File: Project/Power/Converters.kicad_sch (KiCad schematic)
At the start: 24 parts, among them U15 TPS560200, U16 MIC5219-3.3YM5, U17 TPS562200

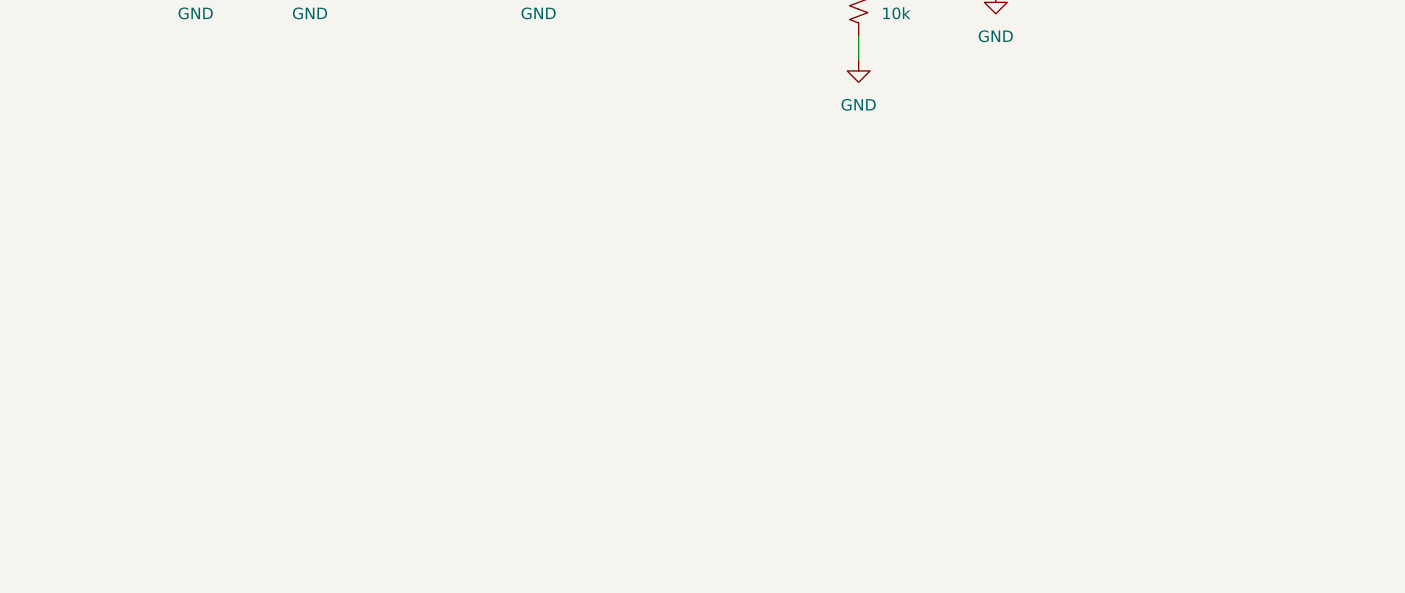
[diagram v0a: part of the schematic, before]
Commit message: Add 5V 6A voltage regulator
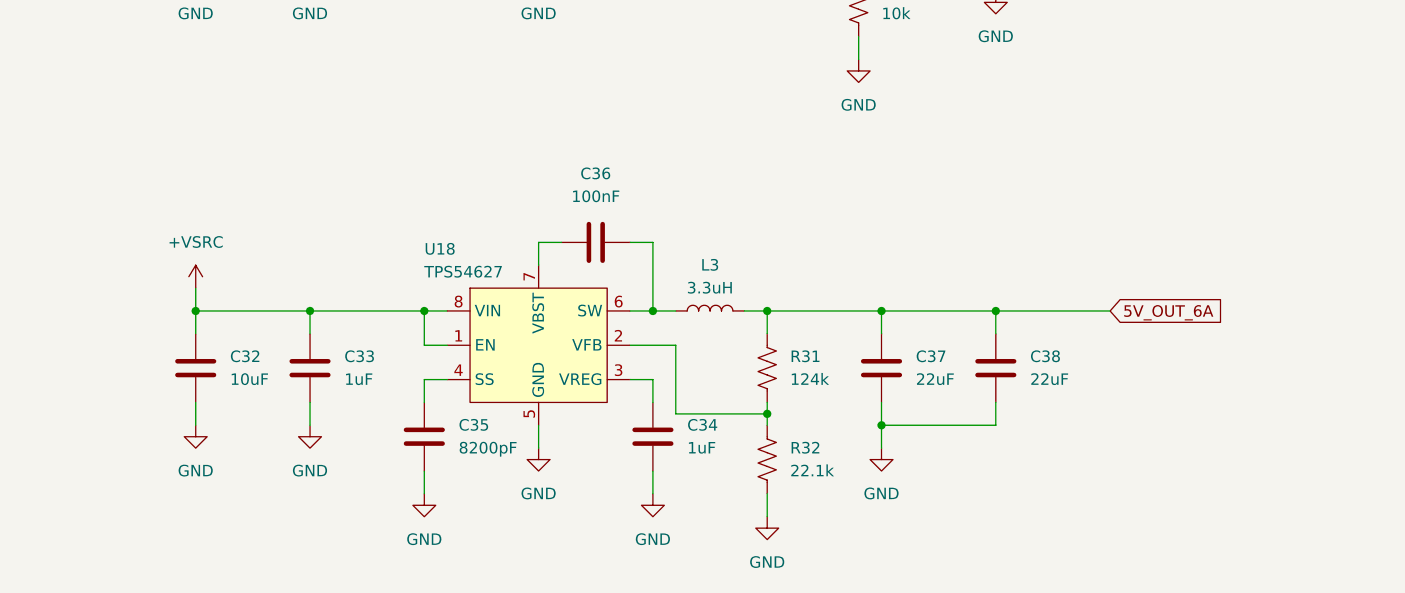
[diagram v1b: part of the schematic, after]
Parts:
- added C32: 10uF, Capacitor_SMD:C_1206_3216Metric, symbol Device:C
- added C33, C34: 1uF, Capacitor_SMD:C_0603_1608Metric, symbol Device:C
- added C35: 8200pF, Capacitor_SMD:C_0603_1608Metric, symbol Device:C
- added C36: 100nF, Capacitor_SMD:C_0603_1608Metric, symbol Device:C
- added C37, C38: 22uF, Capacitor_SMD:C_1206_3216Metric, symbol Device:C
- added L3: 3.3uH, Inductor_SMD:L_APV_APH0630, symbol Device:L
- added R31: 124k, Resistor_SMD:R_0603_1608Metric, symbol Device:R_US
- added R32: 22.1k, Resistor_SMD:R_0603_1608Metric, symbol Device:R_US
- added U18: TPS54627, Package_SO:SOIC-8-1EP_3.9x4.9mm_P1.27mm_EP2.95x4.9mm_Mask2.71x3.4mm_ThermalVias, symbol XuLab:TPS54627
- L2: footprint Inductor_SMD:L_Pulse_PA4340 -> Inductor_SMD:L_APV_APH0630; Listing https://www.digikey.com/en/products/detail/pulse-electronic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 -> https://www.digikey.com/en/products/detail/sumida-america-i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
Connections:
- net +VSRC: now also C32.1, C33.1, U18.1 (EN), U18.8 (VIN)
- net GND: now also C32.2, C33.2, C34.2, C35.2, C37.2, C38.2, R32.1, U18.5 (GND), U18.9 (GND)
- new net: R31.2, R32.2, U18.2 (VFB)
- new net: C34.1, U18.3 (VREG)
- new net: C35.1, U18.4 (SS)
- new net: C36.2, L3.1, U18.6 (SW)
- new net: C36.1, U18.7 (VBST)
- new net 5V_OUT_6A: C37.1, C38.1, L3.2, R31.1

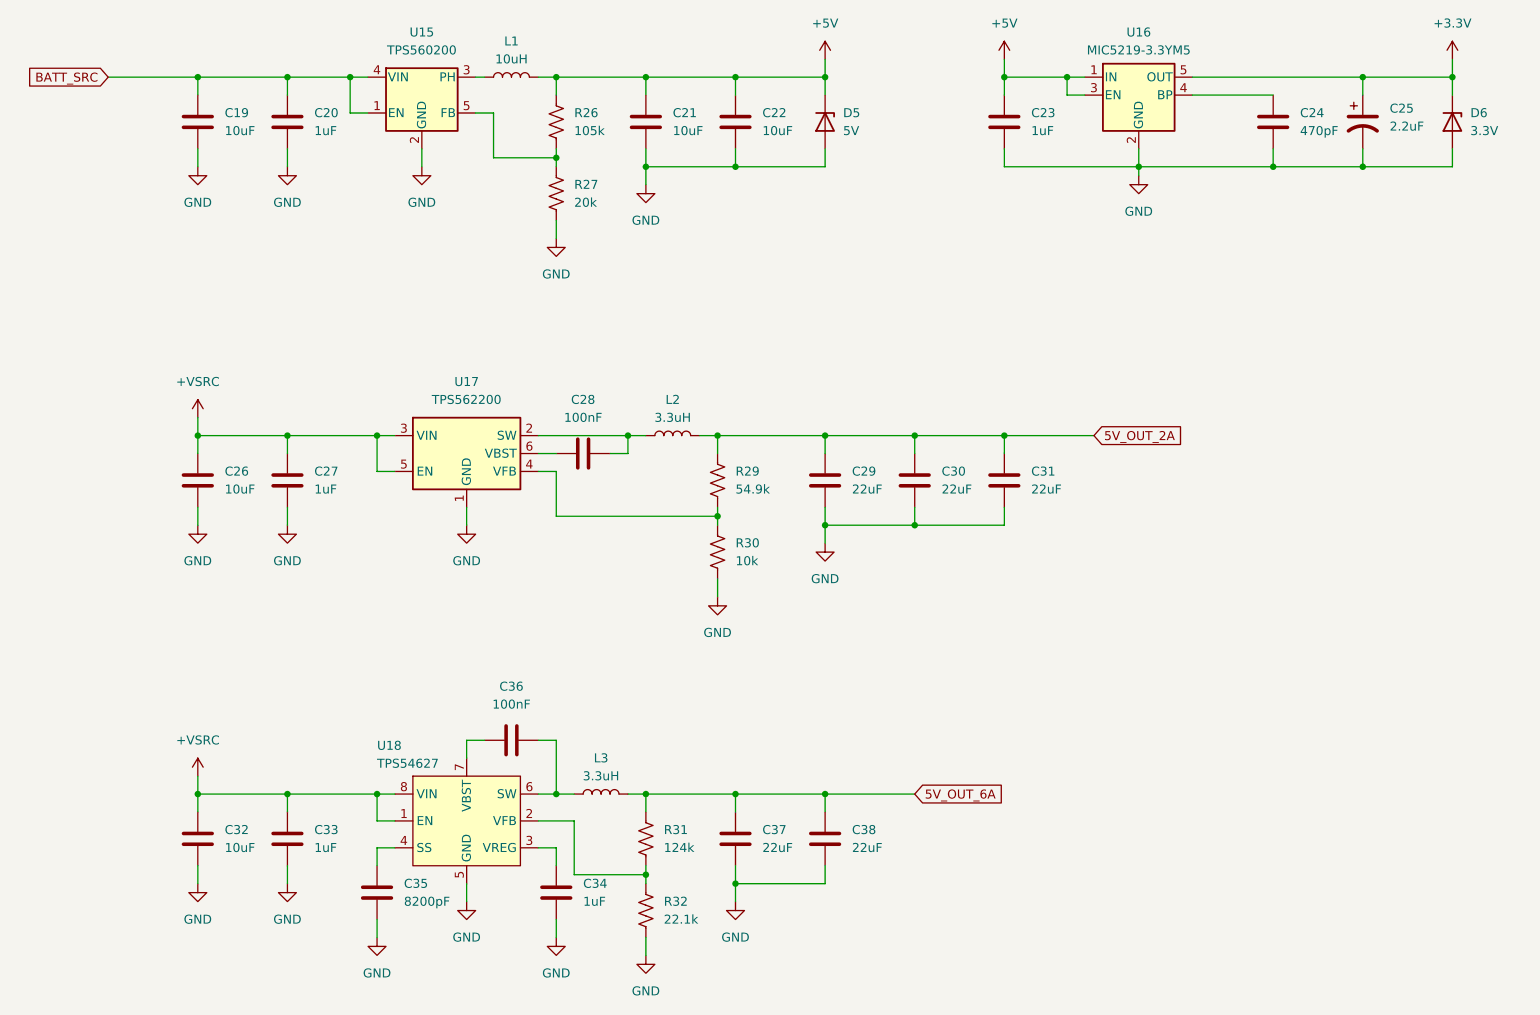
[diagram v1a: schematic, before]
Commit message: Add TVS diodes to switch and converter outputs
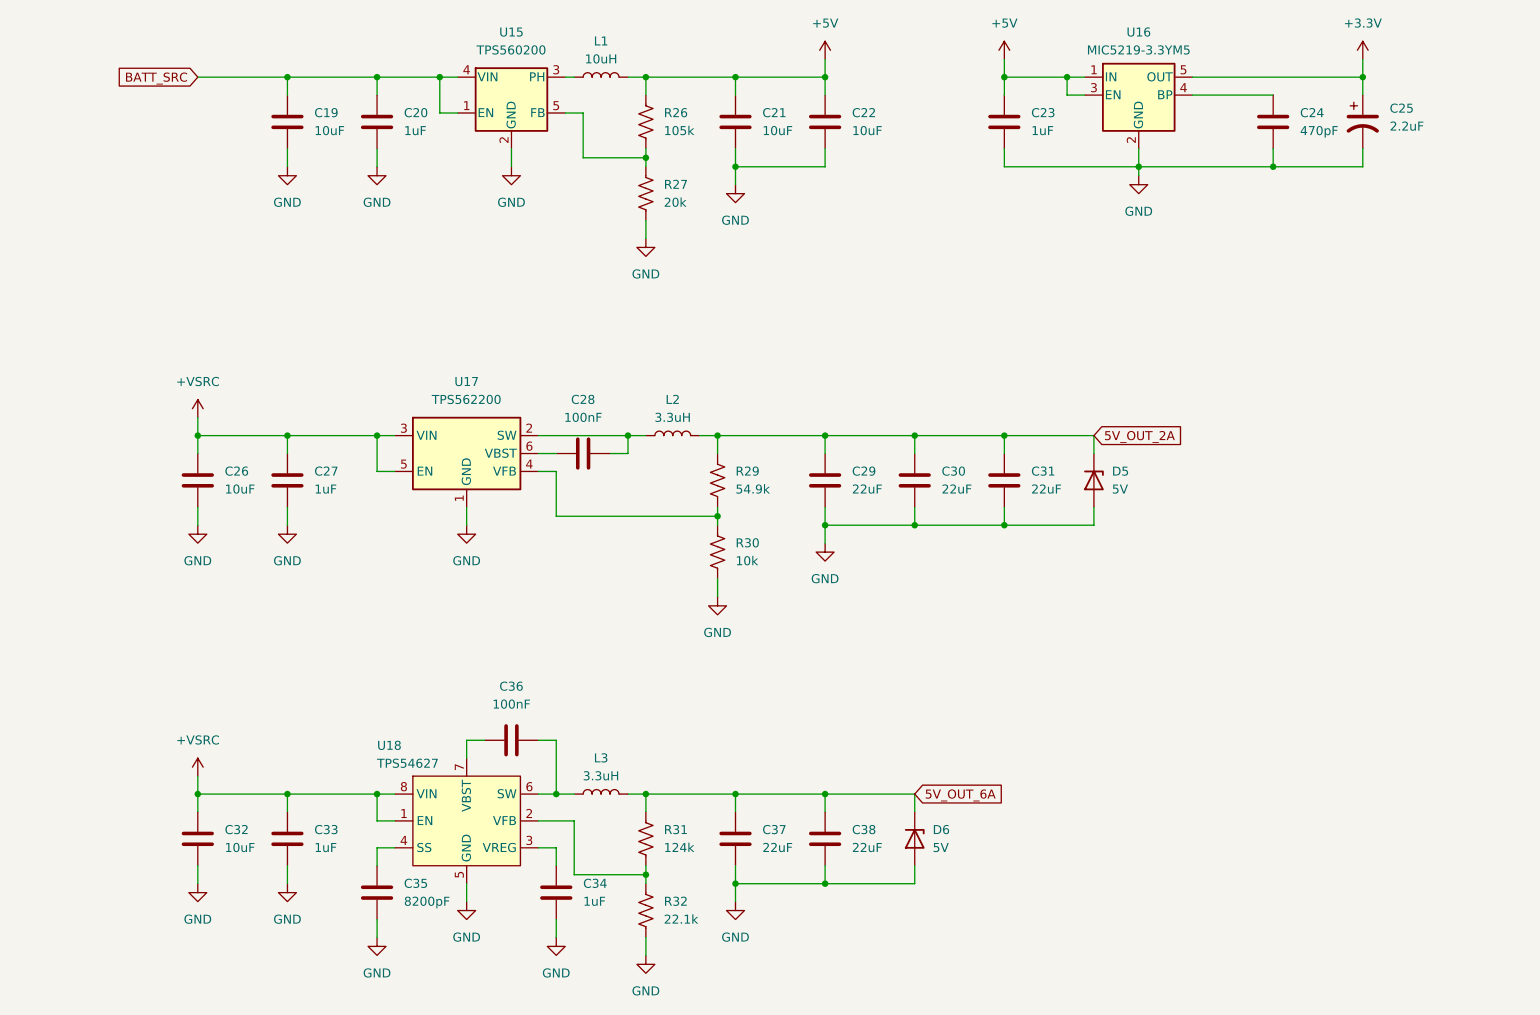
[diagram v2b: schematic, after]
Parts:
- D6: value 3.3V -> 5V; Listing https://www.digikey.com/en/products/detail/vishay-general-semiconductor-diodes-division/MSP3V3-M3-89A/2071748 -> https://www.digikey.com/en/products/detail/vishay-general-semiconductor-diodes-division/MSP5-0A-M3-89A/2071749
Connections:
- net +3.3V: no longer D6.1 (K)
- net +5V: no longer D5.1 (K)
- net 5V_OUT_2A: now also D5.1 (K)
- net 5V_OUT_6A: now also D6.1 (K)
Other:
- moved on the sheet: C19, C20, C21, C22, D5, L1, R26, R27, U15

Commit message: Add converter output connectors
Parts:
- added J16: 5V_2A, Connector_JST:JST_XH_S2B-XH-A_1x02_P2.50mm_Horizontal, symbol Connector_Generic:Conn_01x02
- added J17: 5V_6A, Connector_JST:JST_VH_S2P-VH_1x02_P3.96mm_Horizontal, symbol Connector_Generic:Conn_01x02
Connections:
- net GND: now also J16.2 (Pin_2), J17.2 (Pin_2)
- net 5V_OUT_2A: no longer names the net of C29.1, C30.1, C31.1, D5.1 (K), L2.2, R29.1
- net 5V_OUT_2A: now also J16.1 (Pin_1)
- net 5V_OUT_6A: no longer names the net of C37.1, C38.1, D6.1 (K), L3.2, R31.1
- net 5V_OUT_6A: now also J17.1 (Pin_1)

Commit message: Increase output converter voltage to ~5.1 V
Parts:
- R29: value 54.9k -> 57.6k; Listing https://www.digikey.com/en/products/detail/yageo/RC0603FR-0754K9L/727298 -> https://www.digikey.com/en/products/detail/yageo/RC0603FR-0757K6L/727309
- R31: value 124k -> 127k; Listing https://www.digikey.com/en/products/detail/yageo/RC0603FR-07124KL/726925 -> https://www.digikey.com/en/products/detail/yageo/RC0603FR-07127KL/726927
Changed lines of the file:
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@@
 			)
 		)
-		(property "Value" "124k"
+		(property "Value" "127k"
 			(at 116.84 147.3199 0)
 			(effects
@@
 			)
 		)
-		(property "Listing" "https://www.digikey.com/en/products/detail/yageo/RC0603FR-07124KL/726925"
+		(property "Listing" "https://www.digikey.com/en/products/detail/yageo/RC0603FR-07127KL/726927"
 			(at 114.3 146.05 0)
 			(effects
@@
 			)
 		)
-		(property "Value" "54.9k"
+		(property "Value" "57.6k"
 			(at 127 96.5199 0)
 			(effects
@@
 			)
 		)
-		(property "Listing" "https://www.digikey.com/en/products/detail/yageo/RC0603FR-0754K9L/727298"
+		(property "Listing" "https://www.digikey.com/en/products/detail/yageo/RC0603FR-0757K6L/727309"
 			(at 124.46 95.25 0)
 			(effects

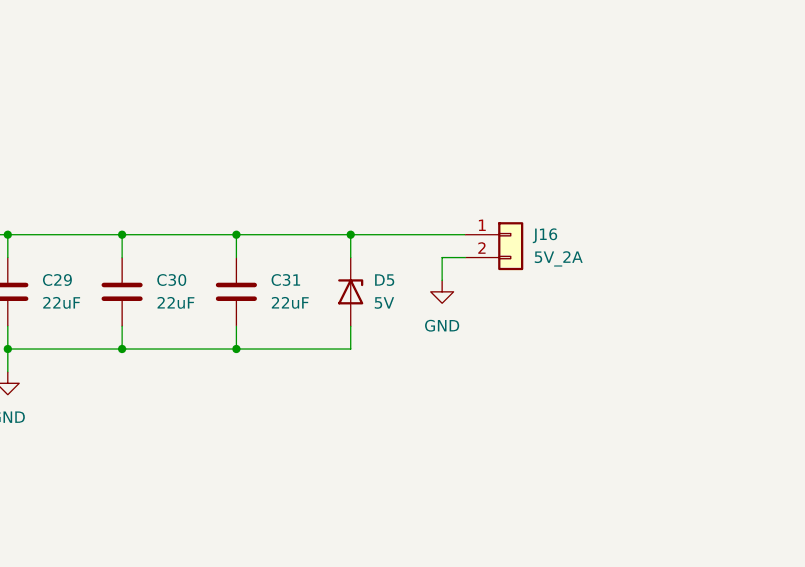
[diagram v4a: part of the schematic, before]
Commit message: Remove extra capacitor in 5V 2A converter
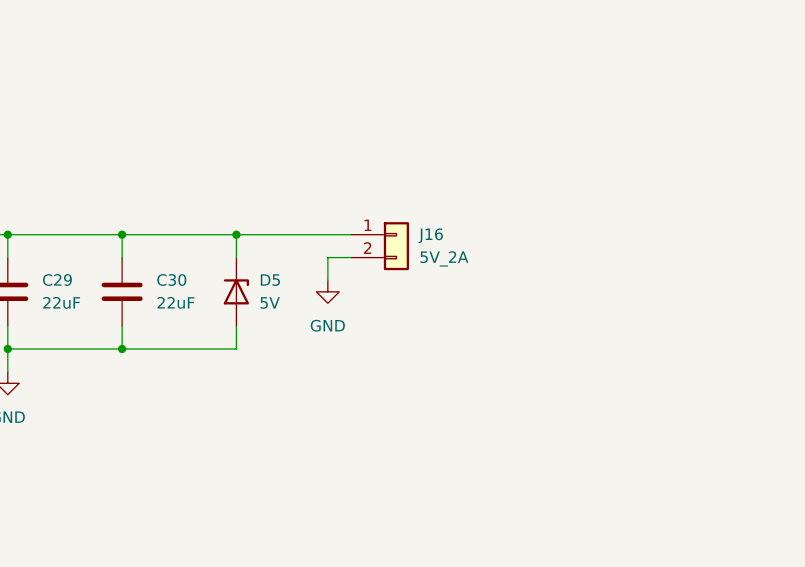
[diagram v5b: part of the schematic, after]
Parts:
- removed C31: 22uF, Capacitor_SMD:C_1206_3216Metric, symbol Device:C
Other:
- moved on the sheet: D5, J16
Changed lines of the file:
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@@
 	)
 	(junction
-		(at 165.1 88.9)
-		(diameter 0)
-		(color 0 0 0 0)
-	)
-	(junction
 		(at 173.99 38.1)
 		(diameter 0)
@@
 	)
 	(junction
-		(at 177.8 88.9)
+		(at 165.1 88.9)
 		(diameter 0)
 		(color 0 0 0 0)
@@
 	)
 	(junction
-		(at 165.1 101.6)
-		(diameter 0)
-		(color 0 0 0 0)
-	)
-	(junction
 		(at 101.6 139.7)
 		(diameter 0)
@@
 	(wire
 		(pts
-			(xy 187.96 91.44) (xy 187.96 93.98)
+			(xy 175.26 91.44) (xy 175.26 93.98)
 		)
 		(stroke
@@
 	(wire
 		(pts
-			(xy 190.5 91.44) (xy 187.96 91.44)
+			(xy 177.8 91.44) (xy 175.26 91.44)
 		)
 		(stroke
@@
 	(wire
 		(pts
-			(xy 165.1 101.6) (xy 177.8 101.6)
+			(xy 152.4 101.6) (xy 165.1 101.6)
 		)
 		(stroke
@@
 	(wire
 		(pts
-			(xy 177.8 88.9) (xy 177.8 91.44)
+			(xy 165.1 88.9) (xy 165.1 91.44)
 		)
 		(stroke
@@
 	(wire
 		(pts
-			(xy 165.1 88.9) (xy 177.8 88.9)
+			(xy 152.4 88.9) (xy 165.1 88.9)
 		)
 		(stroke
@@
 	(wire
 		(pts
-			(xy 152.4 88.9) (xy 165.1 88.9)
-		)
-		(stroke
-			(width 0)
-			(type default)
-		)
-	)
-	(wire
-		(pts
 			(xy 50.8 38.1) (xy 63.5 38.1)
 		)
@@
 	(wire
 		(pts
-			(xy 177.8 99.06) (xy 177.8 101.6)
+			(xy 165.1 99.06) (xy 165.1 101.6)
 		)
 		(stroke
@@
 	(wire
 		(pts
-			(xy 177.8 88.9) (xy 190.5 88.9)
+			(xy 165.1 88.9) (xy 177.8 88.9)
 		)
 		(stroke
@@
 	(wire
 		(pts
-			(xy 165.1 88.9) (xy 165.1 91.44)
-		)
-		(stroke
-			(width 0)
-			(type default)
-		)
-	)
-	(wire
-		(pts
 			(xy 95.25 48.26) (xy 95.25 50.8)
 		)
@@
 	(wire
 		(pts
-			(xy 165.1 99.06) (xy 165.1 101.6)
-		)
-		(stroke
-			(width 0)
-			(type default)
-		)
-	)
-	(wire
-		(pts
 			(xy 99.06 147.32) (xy 101.6 147.32)
 		)
@@
 	(wire
 		(pts
-			(xy 152.4 101.6) (xy 165.1 101.6)
-		)
-		(stroke
-			(width 0)
-			(type default)
-		)
-	)
-	(wire
-		(pts
 			(xy 76.2 88.9) (xy 78.74 88.9)
 		)
@@
 	)
 	(symbol
-		(lib_id "Device:C")
-		(at 165.1 95.25 0)
-		(unit 1)
-		(exclude_from_sim no)
-		(in_bom yes)
-		(on_board yes)
-		(dnp no)
-		(fields_autoplaced yes)
-		(property "Reference" "C31"
-			(at 168.91 93.9799 0)
-			(effects
-				(font
-					(size 1.27 1.27)
-				)
-				(justify left)
-			)
-		)
-		(property "Value" "22uF"
-			(at 168.91 96.5199 0)
-			(effects
-				(font
-					(size 1.27 1.27)
-				)
-				(justify left)
-			)
-		)
-		(property "Footprint" "Capacitor_SMD:C_1206_3216Metric"
-			(at 166.0652 99.06 0)
-			(effects
-				(font
-					(size 1.27 1.27)
-				)
-				(hide yes)
-			)
-		)
-		(property "Datasheet" "https://search.murata.co.jp/Ceramy/image/img/A01X/G101/ENG/GRM31CR71A226KE15-01.pdf"
-			(at 165.1 95.25 0)
-			(effects
-				(font
-					(size 1.27 1.27)
-				)
-				(hide yes)
-			)
-		)
-		(property "Description" "Unpolarized capacitor"
-			(at 165.1 95.25 0)
-			(effects
-				(font
-					(size 1.27 1.27)
-				)
-				(hide yes)
-			)
-		)
-		(property "Listing" "https://www.digikey.com/en/products/detail/murata-electronics/GRM31CR71A226KE15L/2039036"
-			(at 165.1 95.25 0)
-			(effects
-				(font
-					(size 1.27 1.27)
-				)
-				(hide yes)
-			)
-		)
-		(property "Interchangeable" "Yes"
-			(at 165.1 95.25 0)
-			(effects
-				(font
-					(size 1.27 1.27)
-				)
-				(hide yes)
-			)
-		)
-		(pin "1"
-		)
-		(pin "2"
-		)
-		(instances
-			(project "XuLabPower"
-				(path "/71bb14ae-b730-4d22-a41d-cf68989dae2d/39e94aee-ccd8-45cb-a26b-136997d4dd4d"
-					(reference "C31")
-					(unit 1)
-				)
-			)
-		)
-	)
-	(symbol
 		(lib_id "power:GND")
 		(at 88.9 101.6 0)
@@
 	(symbol
 		(lib_id "Connector_Generic:Conn_01x02")
-		(at 195.58 88.9 0)
+		(at 182.88 88.9 0)
 		(unit 1)
 		(exclude_from_sim no)
@@
 		(fields_autoplaced yes)
 		(property "Reference" "J16"
-			(at 198.12 88.8999 0)
+			(at 185.42 88.8999 0)
 			(effects
 				(font
@@
 		)
 		(property "Value" "5V_2A"
-			(at 198.12 91.4399 0)
+			(at 185.42 91.4399 0)
 			(effects
 				(font
@@
 		)
 		(property "Footprint" "Connector_JST:JST_XH_S2B-XH-A_1x02_P2.50mm_Horizontal"
-			(at 195.58 88.9 0)
+			(at 182.88 88.9 0)
 			(effects
 				(font
@@
 		)
 		(property "Datasheet" "https://www.jst-mfg.com/product/pdf/eng/eXH.pdf"
-			(at 195.58 88.9 0)
+			(at 182.88 88.9 0)
 			(effects
 				(font
@@
 		)
 		(property "Description" "Generic connector, single row, 01x02, script generated (kicad-library-utils/schlib/autogen/connector/)"
-			(at 195.58 88.9 0)
+			(at 182.88 88.9 0)
 			(effects
 				(font
@@
 		)
 		(property "Listing" "https://www.digikey.com/en/products/detail/jst-sales-america-inc/S2B-XH-A/1651055"
-			(at 195.58 88.9 0)
+			(at 182.88 88.9 0)
 			(effects
 				(font
@@
 		)
 		(property "Interchangeable" "No"
-			(at 195.58 88.9 0)
+			(at 182.88 88.9 0)
 			(effects
 				(font
@@
 	(symbol
 		(lib_id "power:GND")
-		(at 187.96 93.98 0)
+		(at 175.26 93.98 0)
 		(unit 1)
 		(exclude_from_sim no)
@@
 		(fields_autoplaced yes)
 		(property "Reference" "#PWR0176"
-			(at 187.96 100.33 0)
+			(at 175.26 100.33 0)
 			(effects
 				(font
@@
 		)
 		(property "Value" "GND"
-			(at 187.96 99.06 0)
+			(at 175.26 99.06 0)
 			(effects
 				(font
@@
 		)
 		(property "Footprint" ""
-			(at 187.96 93.98 0)
+			(at 175.26 93.98 0)
 			(effects
 				(font
@@
 		)
 		(property "Datasheet" ""
-			(at 187.96 93.98 0)
+			(at 175.26 93.98 0)
 			(effects
 				(font
@@
 		)
 		(property "Description" "Power symbol creates a global label with name \"GND\" , ground"
-			(at 187.96 93.98 0)
+			(at 175.26 93.98 0)
 			(effects
 				(font
@@
 	(symbol
 		(lib_id "Device:D_Zener")
-		(at 177.8 95.25 270)
+		(at 165.1 95.25 270)
 		(unit 1)
 		(exclude_from_sim no)
@@
 		(fields_autoplaced yes)
 		(property "Reference" "D5"
-			(at 180.34 93.9799 90)
+			(at 167.64 93.9799 90)
 			(effects
 				(font
@@
 		)
 		(property "Value" "5V"
-			(at 180.34 96.5199 90)
+			(at 167.64 96.5199 90)
 			(effects
 				(font
@@
 		)
 		(property "Footprint" "Diode_SMD:D_MicroSMP_KA"
-			(at 177.8 95.25 0)
+			(at 165.1 95.25 0)
 			(effects
 				(font
@@
 		)
 		(property "Datasheet" "https://www.vishay.com/docs/88486/msp3v3.pdf"
-			(at 177.8 95.25 0)
+			(at 165.1 95.25 0)
 			(effects
 				(font
@@
 		)
 		(property "Description" "Zener diode"
-			(at 177.8 95.25 0)
+			(at 165.1 95.25 0)
 			(effects
 				(font
@@
 		)
 		(property "Listing" "https://www.digikey.com/en/products/detail/vishay-general-semiconductor-diodes-division/MSP5-0A-M3-89A/2071749"
-			(at 177.8 95.25 90)
+			(at 165.1 95.25 90)
 			(effects
 				(font
@@
 		)
 		(property "Interchangeable" "Yes"
-			(at 177.8 95.25 90)
+			(at 165.1 95.25 90)
 			(effects
 				(font
